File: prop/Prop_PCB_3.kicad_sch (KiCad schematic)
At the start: 25 parts

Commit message: finalize3pcb schematic
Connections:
- net CS is gone; now on net CS5: U?.10 (~{CS}/SHDN)
- net aData0: now also J?.3
- net aData1: now also J?.3
- net aData2: now also J?.3
- no-connect marks 33 -> 42

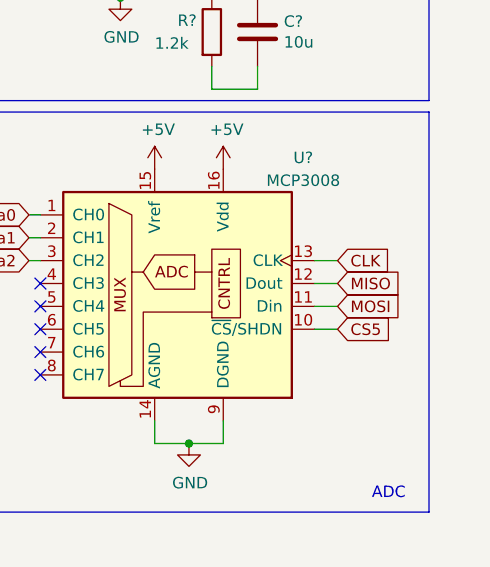
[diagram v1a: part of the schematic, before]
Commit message: fix spelling errors in signals
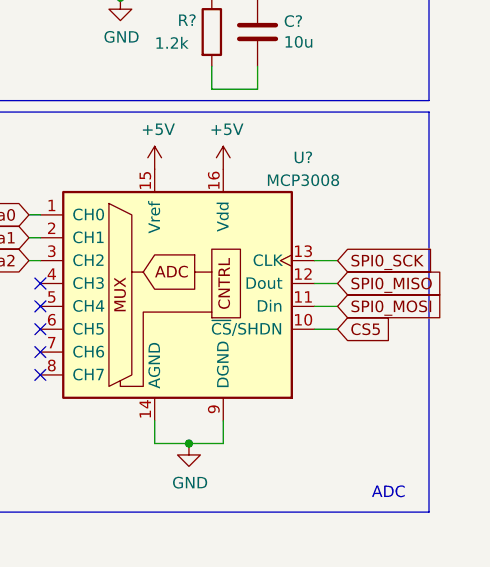
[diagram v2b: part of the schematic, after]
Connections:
- net CLK is gone; now on net SPI0_SCK: U?.13 (CLK)
- net MISO is gone; now on net SPI0_MISO: U?.12 (Dout)
- net MOSI is gone; now on net SPI0_MOSI: U?.11 (Din)
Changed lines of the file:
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@@
     (effects (font (size 1.27 1.27)) (justify left bottom))
   )
-  (global_label "MOSI" (shape input) (at 210.82 104.14 0) (fields_autoplaced)
+  (global_label "SPI0_MOSI" (shape input) (at 210.82 104.14 0) (fields_autoplaced)
     (effects (font (size 1.27 1.27)) (justify left))
-    (property "Intersheet References" "${INTERSHEET_REFS}" (id 0) (at 217.8293 104.0606 0)
+    (property "Intersheet References" "${INTERSHEET_REFS}" (id 0) (at 223.0907 104.0606 0)
       (effects (font (size 1.27 1.27)) (justify left) hide)
     )
@@
     )
   )
-  (global_label "MISO" (shape input) (at 210.82 101.6 0) (fields_autoplaced)
+  (global_label "SPI0_MISO" (shape input) (at 210.82 101.6 0) (fields_autoplaced)
     (effects (font (size 1.27 1.27)) (justify left))
-    (property "Intersheet References" "${INTERSHEET_REFS}" (id 0) (at 217.8293 101.5206 0)
+    (property "Intersheet References" "${INTERSHEET_REFS}" (id 0) (at 223.0907 101.5206 0)
       (effects (font (size 1.27 1.27)) (justify left) hide)
     )
   )
-  (global_label "CLK" (shape input) (at 210.82 99.06 0) (fields_autoplaced)
+  (global_label "SPI0_SCK" (shape input) (at 210.82 99.06 0) (fields_autoplaced)
     (effects (font (size 1.27 1.27)) (justify left))
-    (property "Intersheet References" "${INTERSHEET_REFS}" (id 0) (at 216.8012 98.9806 0)
+    (property "Intersheet References" "${INTERSHEET_REFS}" (id 0) (at 222.2441 98.9806 0)
       (effects (font (size 1.27 1.27)) (justify left) hide)
     )

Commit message: PCB_3 layout ongoing
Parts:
- gave numbers to parts that had none: 25
